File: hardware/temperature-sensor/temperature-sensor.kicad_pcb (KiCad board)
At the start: 2 copper layers, 56 x 56 mm, 87 parts, among them IC1 SHT40-CD1B-R3, IC2 MAX5969BETB+T, IC3 LV2862XLVDDCR, IC4 LV2862XLVDDCR, J1 1149611, J2 219320-0001, J3 1990012, Q1 DMN3404L, T1 SM13126PEL, U1 STM32F407V_E-G_Tx, U2 LAN8720A, U3 FT230XS, Y1 CX2016FB25000C0FZZH1

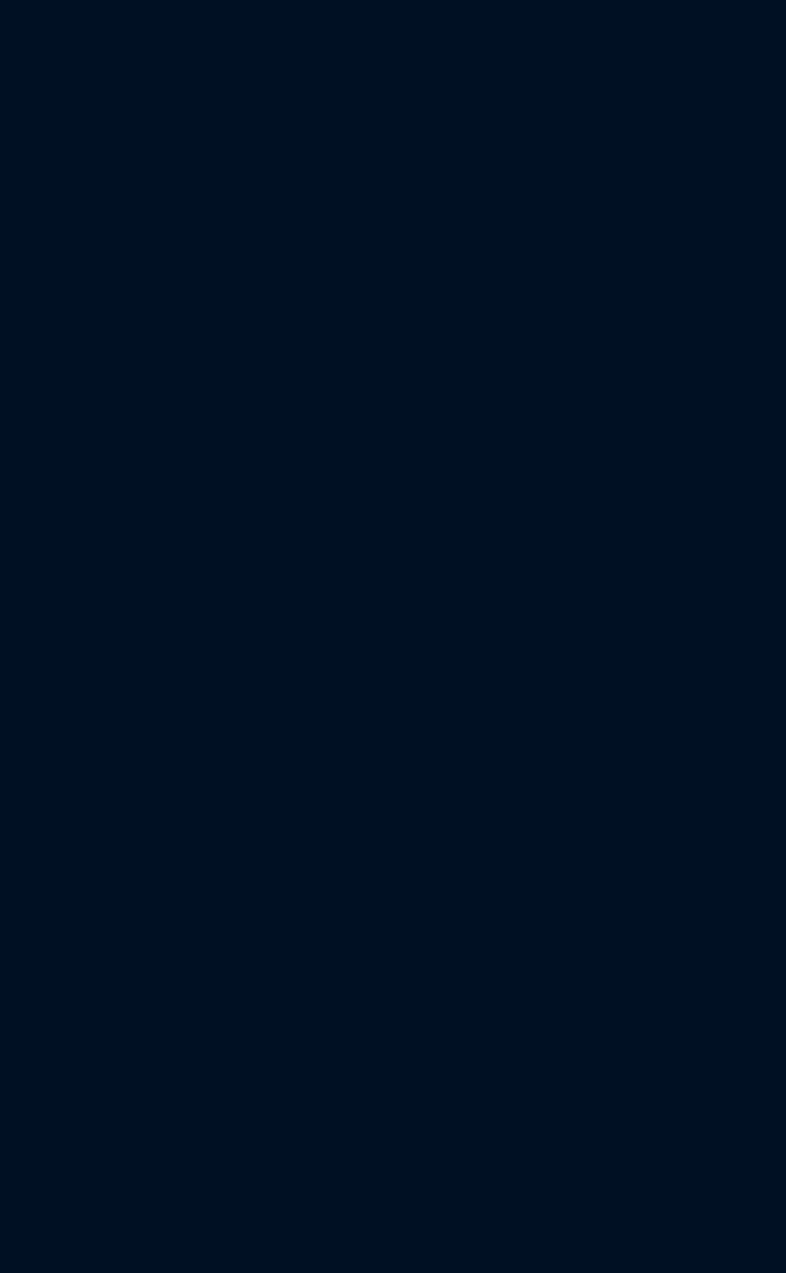
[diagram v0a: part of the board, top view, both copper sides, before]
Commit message: work on temperature sensor
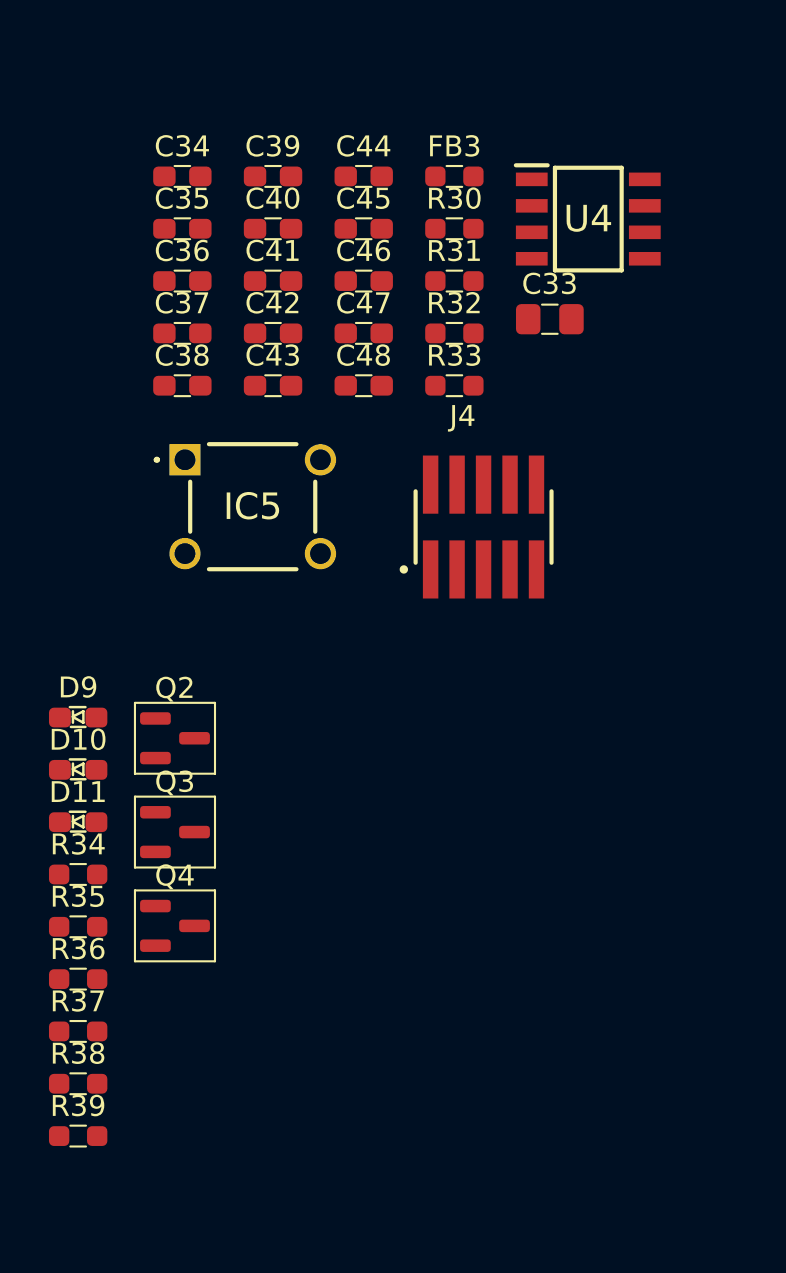
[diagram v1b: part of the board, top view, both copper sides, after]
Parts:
- added C33: 4.7uF, benediktibk:C_0805_2012Metric_Pad1.18x1.45mm_HandSolder, F.Cu at (43.6, 96.3)
- added C34: 100nF, benediktibk:C_0603_1608Metric_Pad1.08x0.95mm_HandSolder, F.Cu at (26.0, 89.5)
- added C35: 100nF, benediktibk:C_0603_1608Metric_Pad1.08x0.95mm_HandSolder, F.Cu at (26.0, 92.0)
- added C36: 100nF, benediktibk:C_0603_1608Metric_Pad1.08x0.95mm_HandSolder, F.Cu at (26.0, 94.5)
- added C37: 100nF, benediktibk:C_0603_1608Metric_Pad1.08x0.95mm_HandSolder, F.Cu at (26.0, 97.0)
- added C38: 100nF, benediktibk:C_0603_1608Metric_Pad1.08x0.95mm_HandSolder, F.Cu at (26.0, 99.5)
- added C39: 100nF, benediktibk:C_0603_1608Metric_Pad1.08x0.95mm_HandSolder, F.Cu at (30.4, 89.5)
- added C40: 100nF, benediktibk:C_0603_1608Metric_Pad1.08x0.95mm_HandSolder, F.Cu at (30.4, 92.0)
- added C41: 100nF, benediktibk:C_0603_1608Metric_Pad1.08x0.95mm_HandSolder, F.Cu at (30.4, 94.5)
- added C42: 1uF, benediktibk:C_0603_1608Metric_Pad1.08x0.95mm_HandSolder, F.Cu at (30.4, 97.0)
- added C43: 1uF, benediktibk:C_0603_1608Metric_Pad1.08x0.95mm_HandSolder, F.Cu at (30.4, 99.5)
- added C44: 100nF, benediktibk:C_0603_1608Metric_Pad1.08x0.95mm_HandSolder, F.Cu at (34.7, 89.5)
- added C45: 2.2uF, benediktibk:C_0603_1608Metric_Pad1.08x0.95mm_HandSolder, F.Cu at (34.7, 92.0)
- added C46: 2.2uF, benediktibk:C_0603_1608Metric_Pad1.08x0.95mm_HandSolder, F.Cu at (34.7, 94.5)
- added C47: 100nF, benediktibk:C_0603_1608Metric_Pad1.08x0.95mm_HandSolder, F.Cu at (34.7, 97.0)
- added C48: 100nF, benediktibk:C_0603_1608Metric_Pad1.08x0.95mm_HandSolder, F.Cu at (34.7, 99.5)
- added D10: red, benediktibk:D_0603_1608Metric_Pad1.05x0.95mm_HandSolder, F.Cu at (21.0, 117.9)
- added D11: yellow, benediktibk:D_0603_1608Metric_Pad1.05x0.95mm_HandSolder, F.Cu at (21.0, 120.4)
- added D9: green, benediktibk:D_0603_1608Metric_Pad1.05x0.95mm_HandSolder, F.Cu at (21.0, 115.4)
- added FB3: BLM18P, benediktibk:R_0603_1608Metric_Pad0.98x0.95mm_HandSolder, F.Cu at (39.0, 89.5)
- added IC5: RESET, benediktibk:TS026650BK100SCRD, F.Cu at (26.1, 103.1)
- added J4: ARM-JTAG-SWD, benediktibk:SAMTEC_FTSH-105-01-F-DV-P-TR, F.Cu at (40.5, 106.3)
- added Q2: DMN3404L, benediktibk:SOT-23, F.Cu at (25.6, 116.4)
- added Q3: DMN3404L, benediktibk:SOT-23, F.Cu at (25.6, 120.9)
- added Q4: DMN3404L, benediktibk:SOT-23, F.Cu at (25.6, 125.4)
- added R30: 10kOhm, benediktibk:R_0603_1608Metric_Pad0.98x0.95mm_HandSolder, F.Cu at (39.0, 92.0)
- added R31: 10kOhm, benediktibk:R_0603_1608Metric_Pad0.98x0.95mm_HandSolder, F.Cu at (39.0, 94.5)
- added R32: 4.7kOhm, benediktibk:R_0603_1608Metric_Pad0.98x0.95mm_HandSolder, F.Cu at (39.0, 97.0)
- added R33: 4.7kOhm, benediktibk:R_0603_1608Metric_Pad0.98x0.95mm_HandSolder, F.Cu at (39.0, 99.5)
- added R34: 10kOhm, benediktibk:R_0603_1608Metric_Pad0.98x0.95mm_HandSolder, F.Cu at (21.0, 123.0)
- added R35: 100Ohm, benediktibk:R_0603_1608Metric_Pad0.98x0.95mm_HandSolder, F.Cu at (21.0, 125.5)
- added R36: 10kOhm, benediktibk:R_0603_1608Metric_Pad0.98x0.95mm_HandSolder, F.Cu at (21.0, 128.0)
- added R37: 100Ohm, benediktibk:R_0603_1608Metric_Pad0.98x0.95mm_HandSolder, F.Cu at (21.0, 130.5)
- added R38: 10kOhm, benediktibk:R_0603_1608Metric_Pad0.98x0.95mm_HandSolder, F.Cu at (21.0, 133.0)
- added R39: 100Ohm, benediktibk:R_0603_1608Metric_Pad0.98x0.95mm_HandSolder, F.Cu at (21.0, 135.5)
- added U4: AT24C512C, benediktibk:SOIC127P600X175-8N, F.Cu at (45.5, 91.5)
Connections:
- U1 pad 10: Net-(U1-VSS-Pad10) -> GND
- U1 pad 100: unconnected-(U1-VDD-Pad100) -> /3V3
- U1 pad 11: unconnected-(U1-VDD-Pad11) -> /3V3
- U1 pad 14: unconnected-(U1-NRST-Pad14) -> /MCU/NRST
- U1 pad 16: unconnected-(U1-PC1-Pad16) -> /Ethernet/MDC
- U1 pad 19: unconnected-(U1-VDD-Pad19) -> /3V3
- U1 pad 20: unconnected-(U1-VSSA-Pad20) -> GND
- U1 pad 21: unconnected-(U1-VREF+-Pad21) -> /MCU/VDDA
- U1 pad 22: unconnected-(U1-VDDA-Pad22) -> /MCU/VDDA
- U1 pad 23: unconnected-(U1-PA0-Pad23) -> /Fan/TACH
- U1 pad 24: unconnected-(U1-PA1-Pad24) -> /Ethernet/nRST
- U1 pad 25: unconnected-(U1-PA2-Pad25) -> /Ethernet/MDIO
- U1 pad 26: unconnected-(U1-PA3-Pad26) -> /MCU/LED1
- U1 pad 27: Net-(U1-VSS-Pad10) -> GND
- U1 pad 28: unconnected-(U1-VDD-Pad28) -> /3V3
- U1 pad 29: unconnected-(U1-PA4-Pad29) -> /MCU/LED2
- U1 pad 30: unconnected-(U1-PA5-Pad30) -> /MCU/LED3
- U1 pad 31: unconnected-(U1-PA6-Pad31) -> /Fan/PWM
- U1 pad 32: unconnected-(U1-PA7-Pad32) -> /Ethernet/CRS_DV/MODE2
- U1 pad 33: unconnected-(U1-PC4-Pad33) -> /Ethernet/RXD0/MODE0
- U1 pad 34: unconnected-(U1-PC5-Pad34) -> /Ethernet/RXD1/MODE1
- U1 pad 47: unconnected-(U1-PB10-Pad47) -> /Ethernet/RXER/PHYAD0
- U1 pad 48: unconnected-(U1-PB11-Pad48) -> /Ethernet/TXEN
- U1 pad 49: unconnected-(U1-VCAP_1-Pad49) -> Net-(U1-VCAP_1)
- U1 pad 50: unconnected-(U1-VDD-Pad50) -> /3V3
- U1 pad 51: unconnected-(U1-PB12-Pad51) -> /Ethernet/TXD0
- U1 pad 52: unconnected-(U1-PB13-Pad52) -> /Ethernet/TXD1
- U1 pad 6: unconnected-(U1-VBAT-Pad6) -> /3V3
- U1 pad 67: unconnected-(U1-PA8-Pad67) -> /Ethernet/25MHz
- U1 pad 72: unconnected-(U1-PA13-Pad72) -> /MCU/SWDIO
- U1 pad 73: unconnected-(U1-VCAP_2-Pad73) -> Net-(U1-VCAP_2)
- U1 pad 74: Net-(U1-VSS-Pad10) -> GND
- U1 pad 75: unconnected-(U1-VDD-Pad75) -> /3V3
- U1 pad 76: unconnected-(U1-PA14-Pad76) -> /MCU/SWCLK
- U1 pad 92: unconnected-(U1-PB6-Pad92) -> /MCU/UART_TX
- U1 pad 93: unconnected-(U1-PB7-Pad93) -> /MCU/UART_RX
- U1 pad 94: unconnected-(U1-BOOT0-Pad94) -> Net-(U1-BOOT0)
- U1 pad 95: unconnected-(U1-PB8-Pad95) -> /MCU/SCL
- U1 pad 96: unconnected-(U1-PB9-Pad96) -> /MCU/SDA
- U1 pad 99: Net-(U1-VSS-Pad10) -> GND

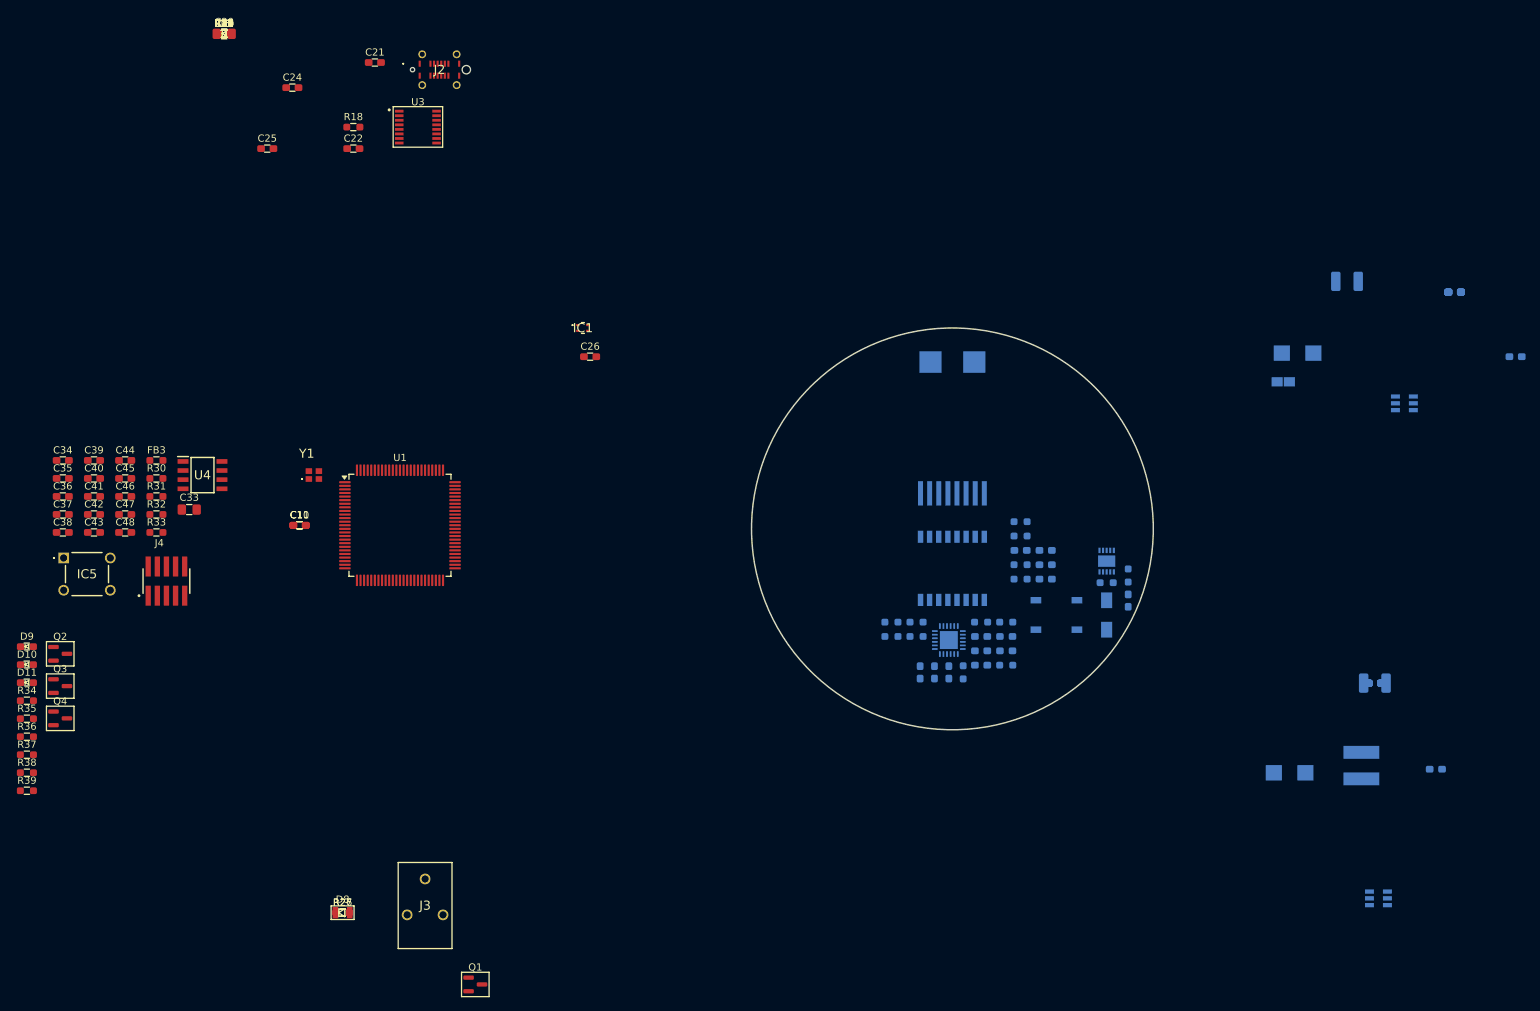
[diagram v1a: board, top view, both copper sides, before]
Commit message: place components of PoE
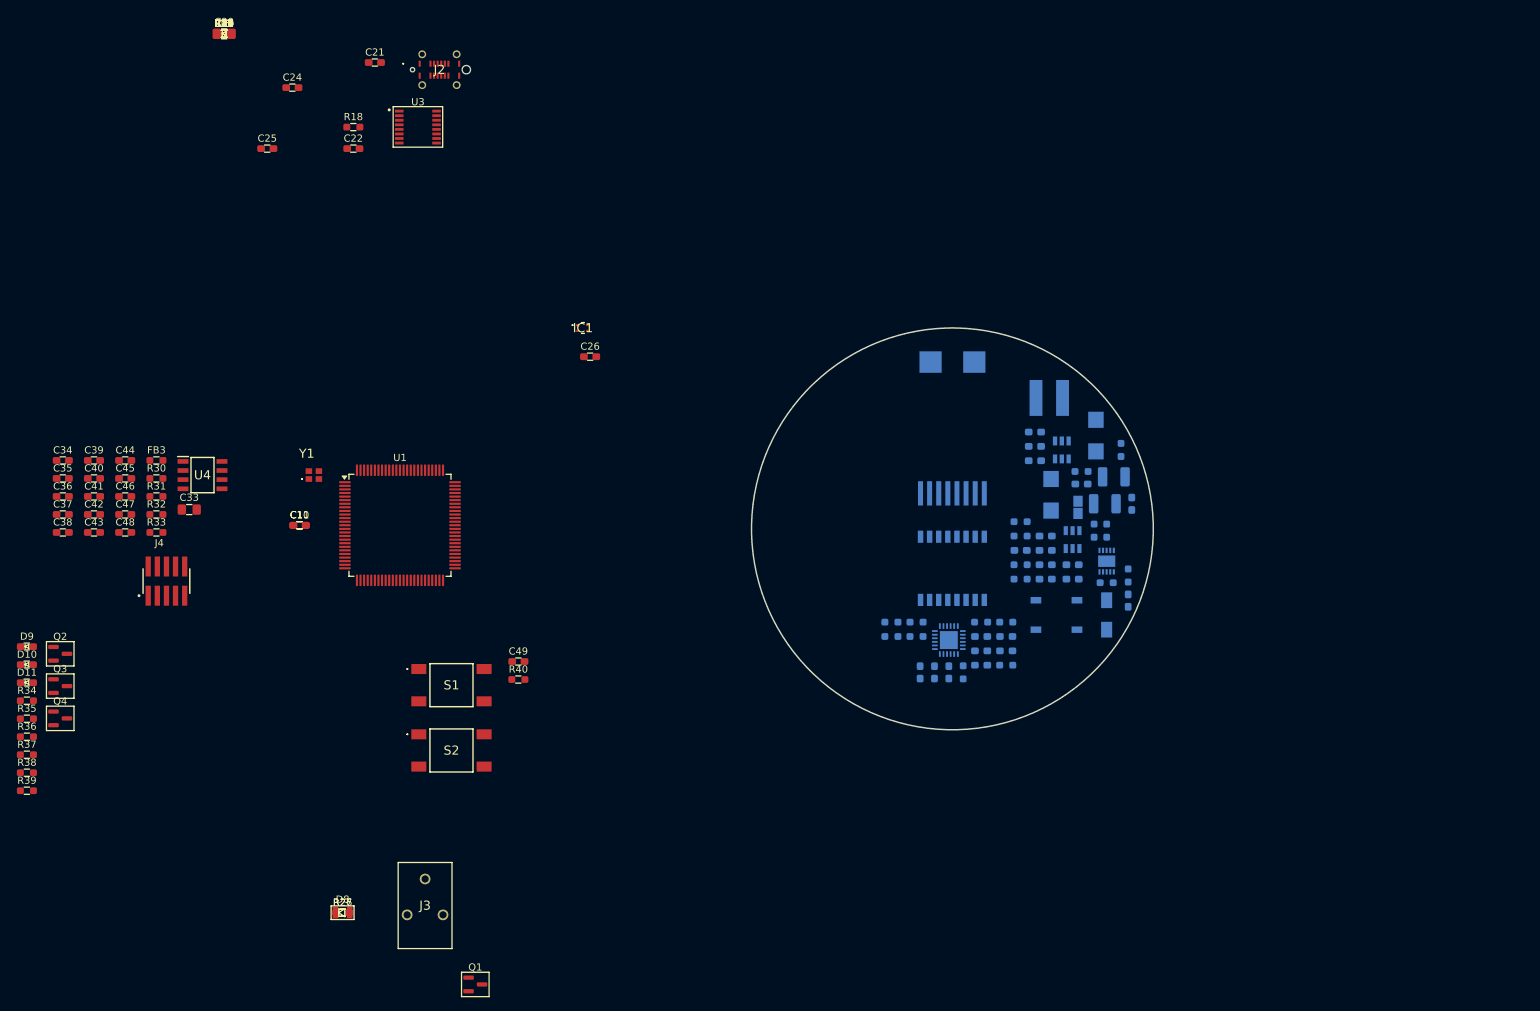
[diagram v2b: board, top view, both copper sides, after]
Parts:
- removed IC5: RESET, benediktibk:TS026650BK100SCRD
- added C49: 100nF, benediktibk:C_0603_1608Metric_Pad1.08x0.95mm_HandSolder, F.Cu at (89.5, 117.5)
- added R40: 10kOhm, benediktibk:R_0603_1608Metric_Pad0.98x0.95mm_HandSolder, F.Cu at (89.5, 120.0)
- added S1: RESET, benediktibk:TS046673BK100SMT, F.Cu at (80.2, 120.8)
- added S2: RESET, benediktibk:TS046673BK100SMT, F.Cu at (80.2, 129.9)
- moved IC3 76.5 mm to (165.2, 88.0), turned to -90 degrees
- moved C3 71.7 mm to (161.5, 87.5), turned to 0 degrees
- moved C29 69.1 mm to (166.8, 106.0)
- moved L1 67.2 mm to (163.5, 80.8), turned to 90 degrees
- moved C27 66.4 mm to (163.0, 100.0)
- moved C28 65.4 mm to (166.8, 104.0)
- moved R24 60.3 mm to (169.8, 99.2), turned to -90 degrees
- moved C13 58.9 mm to (161.5, 85.5), turned to 0 degrees
- moved R25 58.8 mm to (171.5, 99.2), turned to 90 degrees
- moved C31 58.5 mm to (168.0, 92.8), turned to 0 degrees
- moved C2 56.6 mm to (161.5, 89.5), turned to 0 degrees
- moved D4 54.2 mm to (170.0, 86.0), turned to -90 degrees
- moved R12 50.4 mm to (168.0, 91.0)
- moved IC4 50.0 mm to (166.8, 100.5), turned to -90 degrees
- moved R13 48.0 mm to (173.5, 88.0), turned to 90 degrees
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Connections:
- U1 pad 68: unconnected-(U1-PA9-Pad68) -> /MCU/CONNECT
